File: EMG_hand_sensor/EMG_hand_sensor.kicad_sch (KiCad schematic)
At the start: 53 parts, among them J1 USB_C_Receptacle_USB2.0_16P, J2 Conn_01x04_Pin, J4 AudioJack3, J5 AudioJack3, J6 AudioJack3, SW1 SW_SPDT, U1 USBLC6-2SC6, U2 STM32F103C8Tx, U3 INA128, U5 INA128, U7 LT1762, U9 INA128, Y1 16MHz

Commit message: need to change some things because jlcpcb stock
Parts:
- C10: footprint Capacitor_THT:CP_Radial_D6.3mm_P2.50mm -> Capacitor_THT:CP_Radial_D4.0mm_P2.00mm
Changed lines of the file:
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@@
 			)
 		)
-		(property "Footprint" "Capacitor_THT:CP_Radial_D6.3mm_P2.50mm"
+		(property "Footprint" "Capacitor_THT:CP_Radial_D4.0mm_P2.00mm"
 			(at 255.27 104.14 0)
 			(effects

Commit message: some changes
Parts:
- FB1: footprint Resistor_SMD:R_0805_2012Metric_Pad1.20x1.40mm_HandSolder -> Ferrite_THT:LairdTech_28C0236-0JW-10
- RV1, RV2, RV3: footprint Potentiometer_SMD:Potentiometer_Bourns_3214W_Vertical -> Potentiometer_SMD:Potentiometer_Bourns_3214J_Horizontal
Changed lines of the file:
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@@
 			)
 		)
-		(property "Footprint" "Potentiometer_SMD:Potentiometer_Bourns_3214W_Vertical"
+		(property "Footprint" "Potentiometer_SMD:Potentiometer_Bourns_3214J_Horizontal"
 			(at 114.3 30.48 0)
 			(effects
@@
 			)
 		)
-		(property "Footprint" "Potentiometer_SMD:Potentiometer_Bourns_3214W_Vertical"
+		(property "Footprint" "Potentiometer_SMD:Potentiometer_Bourns_3214J_Horizontal"
 			(at 173.99 87.63 0)
 			(effects
@@
 			)
 		)
-		(property "Footprint" "Resistor_SMD:R_0805_2012Metric_Pad1.20x1.40mm_HandSolder"
+		(property "Footprint" "Ferrite_THT:LairdTech_28C0236-0JW-10"
 			(at 134.62 57.912 90)
 			(effects
@@
 			)
 		)
-		(property "Footprint" "Potentiometer_SMD:Potentiometer_Bourns_3214W_Vertical"
+		(property "Footprint" "Potentiometer_SMD:Potentiometer_Bourns_3214J_Horizontal"
 			(at 234.95 60.96 0)
 			(effects

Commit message: looks good
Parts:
- FB1: footprint Ferrite_THT:LairdTech_28C0236-0JW-10 -> Ferrite_SMT:BLM21AG102BH1J
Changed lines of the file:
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@@
 			)
 		)
-		(property "Footprint" "Ferrite_THT:LairdTech_28C0236-0JW-10"
+		(property "Footprint" "Ferrite_SMT:BLM21AG102BH1J"
 			(at 134.62 57.912 90)
 			(effects

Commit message: done ordered
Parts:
- C1: Distributor (none) -> https://www.mouser.co.uk/ProductDetail/TDK/C2012X5R1E106M12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; MANUFACTURER (none) -> TDK; Manfacturer_number (none) -> C2012X5R1E106M125AB
- C10: Distributor (none) -> https://www.digikey.co.uk/en/products/detail/panasonic-elec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; MANUFACTURER (none) -> Panasonic Electronic Components; Manfacturer_number (none) -> ECA-0JHG101
- C11, C7: Distributor (none) -> https://www.mouser.co.uk/ProductDetail/KEMET/C0805X103JCRAC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; MANUFACTURER (none) -> KEMET; Manfacturer_number (none) -> C0805X103JCRAC3316
- C12, C8, C9: Distributor (none) -> https://www.mouser.co.uk/ProductDetail/KEMET/C0805X105J5RAC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; MANUFACTURER (none) -> KEMET; Manfacturer_number (none) -> C0805X105J5RACAUTO
- C13, C16, C17, C18, C19, C2, C20, C21, C3, C4, C5, C6: Distributor (none) -> https://www.mouser.co.uk/ProductDetail/Vishay-Vitramon/GA08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; MANUFACTURER (none) -> Vishay / Vitramon; Manfacturer_number (none) -> GA0805Y104KBBBT31G
- C14, C15: Distributor (none) -> https://www.mouser.co.uk/ProductDetail/KEMET/C0805C100KDTAC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; MANUFACTURER (none) -> KEMET; Manfacturer_number (none) -> C0805C100KDTACTU
- D1: Distributor (none) -> https://www.digikey.co.uk/en/products/detail/kingbright/APT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; MANUFACTURER (none) -> Kingbright; Manfacturer_number (none) -> APT2012SURCK
- FB1: Distributor (none) -> https://www.digikey.com/en/products/detail/murata-electroni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; MANUFACTURER (none) -> Murata Electronics; Manfacturer_number (none) -> BLM21AG102SN1D
- FID1, FID2, FID3, H1, H2: now fitted
- J1: Distributor (none) -> https://www.digikey.com/en/products/detail/gct/USB4105-GF-A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; MANUFACTURER (none) -> GCT; Manfacturer_number (none) -> USB4105-GF-A
- J2: Distributor (none) -> https://www.digikey.com/en/products/detail/w%C3%BCrth-elekt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; MANUFACTURER (none) -> Würth Elektronik; Manfacturer_number (none) -> 61300411121
- J4, J5, J6: Distributor (none) -> https://www.digikey.co.uk/en/products/detail/same-sky-forme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; MANUFACTURER (none) -> Same Sky (Formerly CUI Devices); Manfacturer_number (none) -> SJ-3523-SMT-TR
- R1, R3, R4: Distributor (none) -> https://www.digikey.com/en/products/detail/susumu/RR1220P-1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; MANUFACTURER (none) -> Susumu; Manfacturer_number (none) -> RR1220P-103-D
- R11, R12, R14: Distributor (none) -> https://www.digikey.com/en/products/detail/susumu/RG2012L-3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; MANUFACTURER (none) -> Susumu; Manfacturer_number (none) -> RG2012L-332-L-T05
- R2: Distributor (none) -> https://www.digikey.com/en/products/detail/yageo/RC0805JR-0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; MANUFACTURER (none) -> YAGEO; Manfacturer_number (none) -> RC0805JR-071K5L
- R8, R9: Distributor (none) -> https://www.digikey.com/en/products/detail/yageo/RC0402JR-0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; MANUFACTURER (none) -> YAGEO; Manfacturer_number (none) -> RC0402JR-074K7L
- RV1, RV2, RV3: Distributor (none) -> https://www.digikey.com/en/products/detail/bourns-inc/3214J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; MANUFACTURER (none) -> Bourns Inc.; Manfacturer_number (none) -> 3214J-1-103E
- SW1: Distributor (none) -> https://www.digikey.com/en/products/detail/c-k/JS102011SAQN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; MANUFACTURER (none) -> C&K; Manfacturer_number (none) -> JS102011SAQN
- U1: Distributor (none) -> https://www.digikey.com/en/products/detail/stmicroelectroni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; MANUFACTURER (none) -> STMicroelectronics; Manfacturer_number (none) -> USBLC6-2SC6
- U2: value STM32F103C8Tx -> STM32F103C8T6; Distributor (none) -> https://www.digikey.co.uk/en/products/detail/stmicroelectro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; MANUFACTURER (none) -> STMicroelectronics; Manfacturer_number (none) -> STM32F103C8T6
- U3, U5, U9: Distributor (none) -> https://www.digikey.com/en/products/detail/texas-instrument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; MANUFACTURER (none) -> Texas Instruments; Manfacturer_number (none) -> INA128U
- U7: Distributor (none) -> https://www.digikey.com/en/products/detail/analog-devices-i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; MANUFACTURER (none) -> Analog Devices Inc.; Manfacturer_number (none) -> LT1762EMS8-3.3#TRPBF
- Y1: Distributor (none) -> https://www.digikey.com/en/products/detail/epson/TSX-3225-1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; MANUFACTURER (none) -> EPSON; Manfacturer_number (none) -> TSX-3225 16.0000MF10U-B0

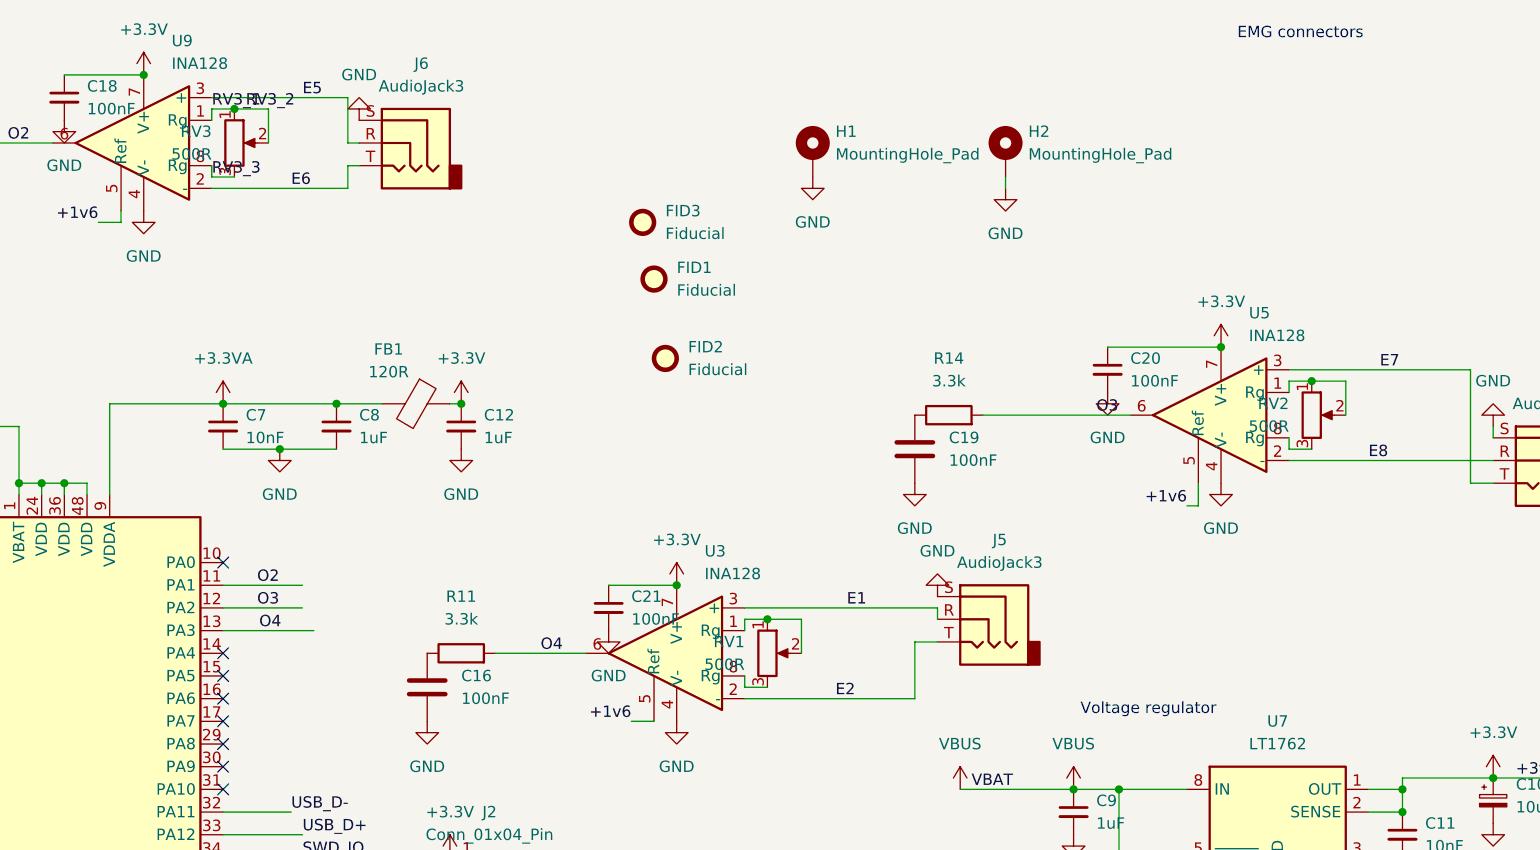
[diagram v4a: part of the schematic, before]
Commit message: updated for cheaper parts
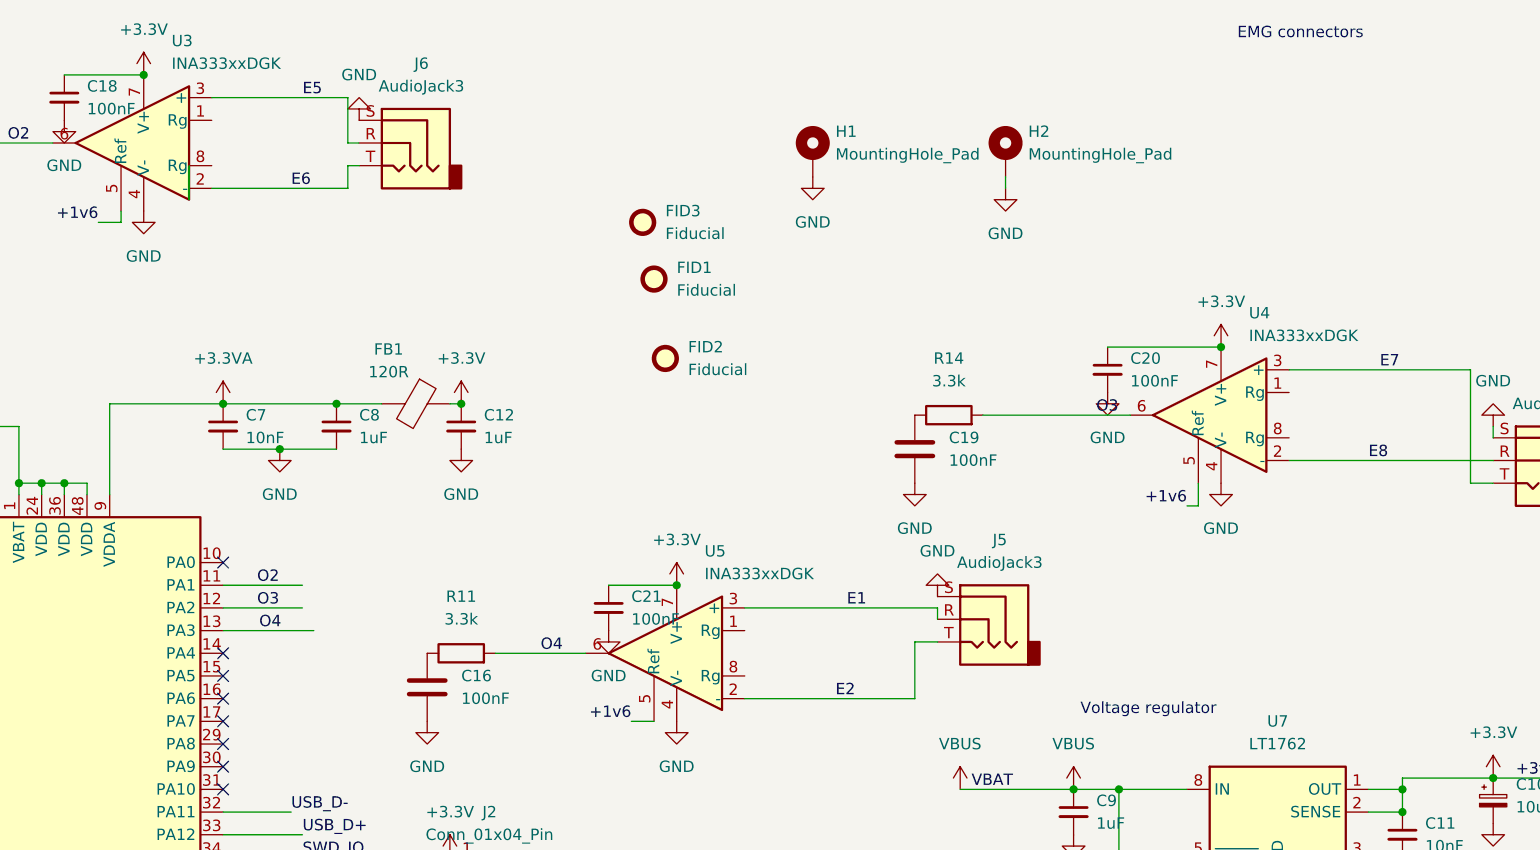
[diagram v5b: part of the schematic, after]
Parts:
- removed RV1, RV2, RV3: 500R, Potentiometer_SMD:Potentiometer_Bourns_3214J_Horizontal, symbol Device:R_Potentiometer
- removed U3, U5, U9: INA128, INA:SOIC127P600X175-8N, symbol Amplifier_Instrumentation:INA128
- added U3, U4, U5: INA333xxDGK, Package_SO:VSSOP-8_3x3mm_P0.65mm, symbol Amplifier_Instrumentation:INA333xxDGK
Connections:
- net +1V6: now also U3.5 (Ref), U4.5 (Ref), U5.5 (Ref)
- net +3.3V: now also U3.7 (V+), U4.7 (V+), U5.7 (V+)
- net E1: now also U5.3 (+)
- net E2: now also U5.2 (-)
- net E5: now also U3.3 (+)
- net E6: now also U3.2 (-)
- net E7: now also U4.3 (+)
- net E8: now also U4.2 (-)
- net GND: now also U3.4 (V-), U4.4 (V-), U5.4 (V-)
- net O2: now also U3.6
- net O3: now also U4.6
- net O4: now also U5.6

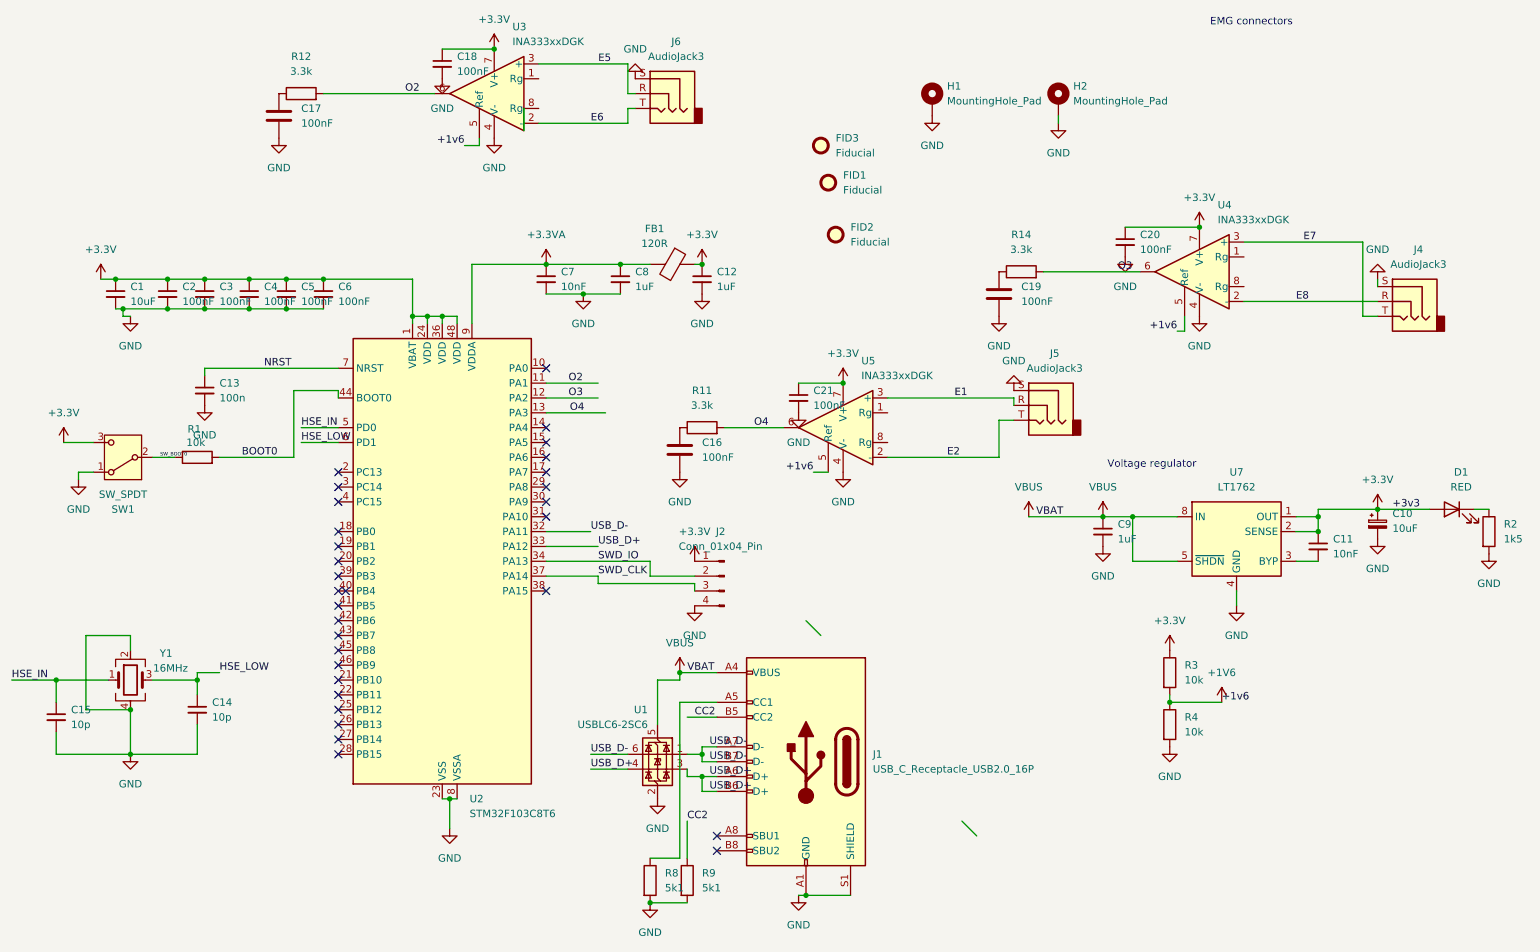
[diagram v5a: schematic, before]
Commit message: ordered boards from jlcpcb
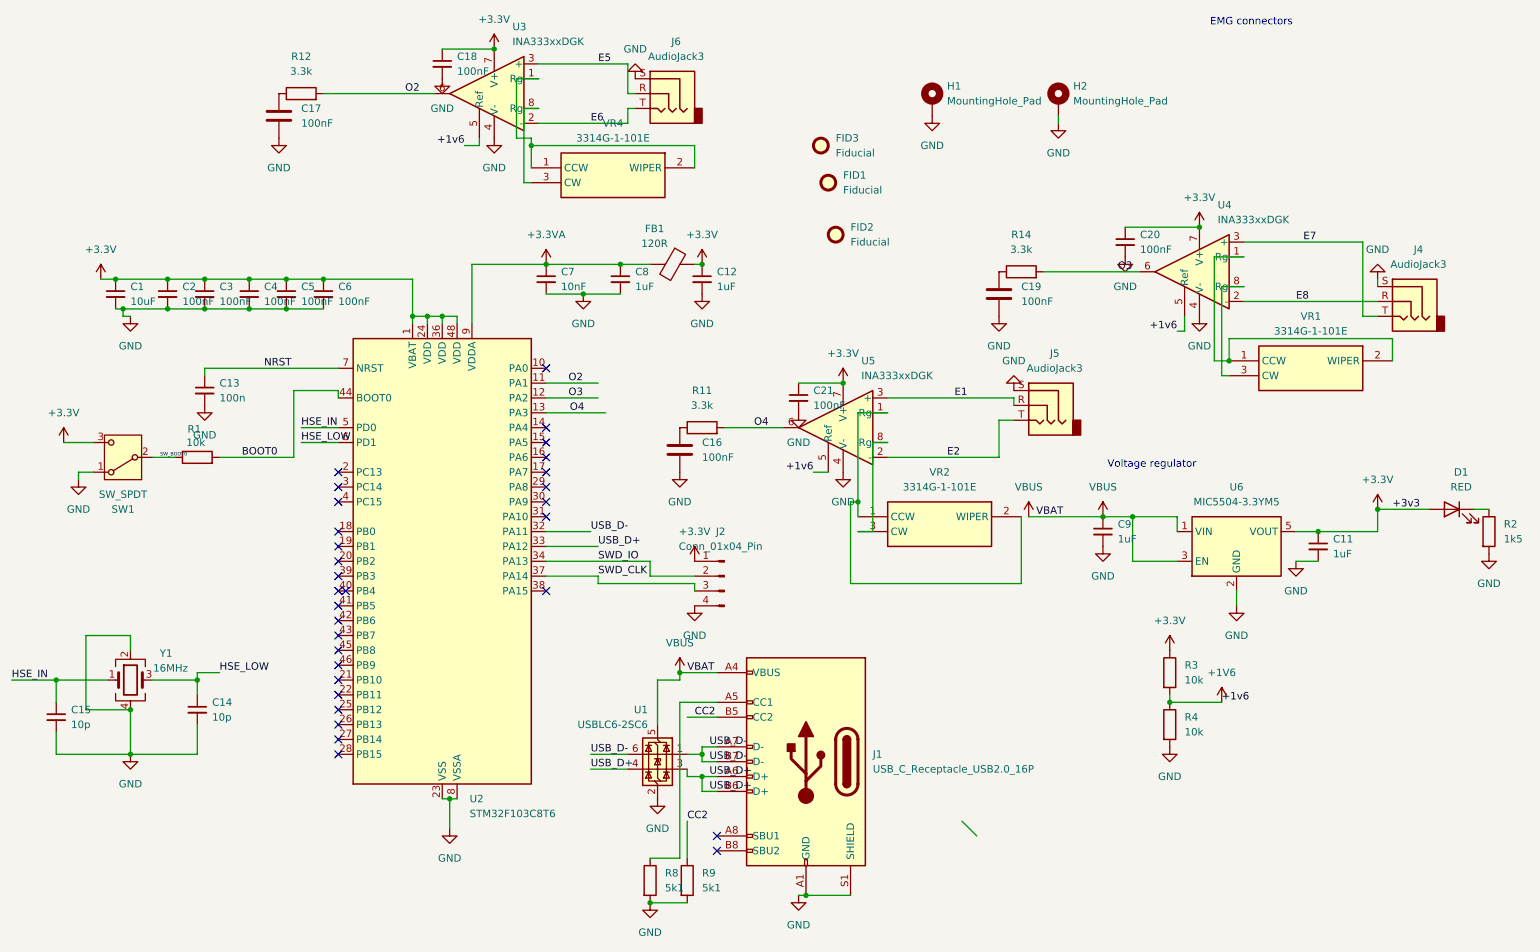
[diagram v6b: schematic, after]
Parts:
- removed C10: 10uF, Capacitor_THT:CP_Radial_D4.0mm_P2.00mm, symbol Device:C_Polarized_Small
- removed U7: LT1762, Package_SO:MSOP-8_3x3mm_P0.65mm, symbol Regulator_Linear:LT1762-3.3
- added U6: MIC5504-3.3YM5, Package_TO_SOT_SMD:SOT-23-5, symbol Regulator_Linear:MIC5504-3.3YM5
- added VR1, VR2, VR4: 3314G-1-101E, Bourne_pot_smd:3314G-1, symbol Bourne_smd_pot:3314G-1-101E
- C11: value 10nF -> 1uF
- U3, U4, U5: Distributor (none) -> https://www.digikey.co.uk/en/products/detail/texas-instrume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; MANUFACTURER (none) -> Texas Instruments; Manfacturer_number (none) -> INA333AIDGKR
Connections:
- net +3.3V: now also U6.5 (VOUT)
- net GND: now also C11.2, U6.2 (GND)
- net VBUS: now also U6.1 (VIN), U6.3 (EN)
- net at U5.1 (Rg): now also VR2.1 (CCW), VR2.2 (WIPER)
- net at U5.8 (Rg): now also VR2.3 (CW)
- net at U4.1 (Rg): now also VR1.1 (CCW), VR1.2 (WIPER)
- net at U4.8 (Rg): now also VR1.3 (CW)
- net at U3.1 (Rg): now also VR4.1 (CCW), VR4.2 (WIPER)
- net at U3.8 (Rg): now also VR4.3 (CW)
